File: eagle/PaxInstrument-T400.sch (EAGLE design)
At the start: 113 parts, among them IC1 MCP3424, J1 MICRO-SDCARD-CONNECTOR-330006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, U1 MCP9800, U3 MCP73831, U4 MIC5219-3.3V, U8 NC7S32, X1 FH12-12S-0.5SH, Y1 RESONATORSMD

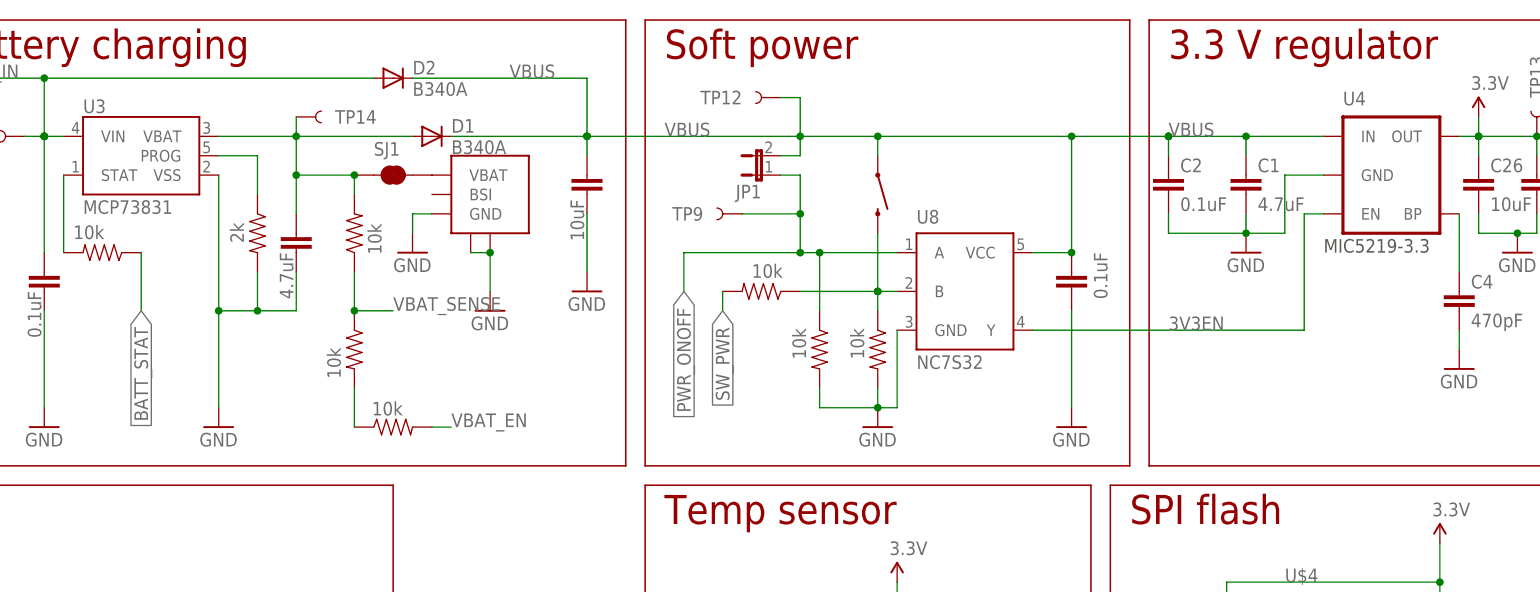
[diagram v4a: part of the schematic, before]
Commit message: Updated Rev 0.10 schematic and library
- What test points are needed? #37 (Added test point for BATT_STAT,
VBAT_SENSE, VBAT_EN -3V3EN in schematic)
- New soft power circuit #134 (Updated schematic only)
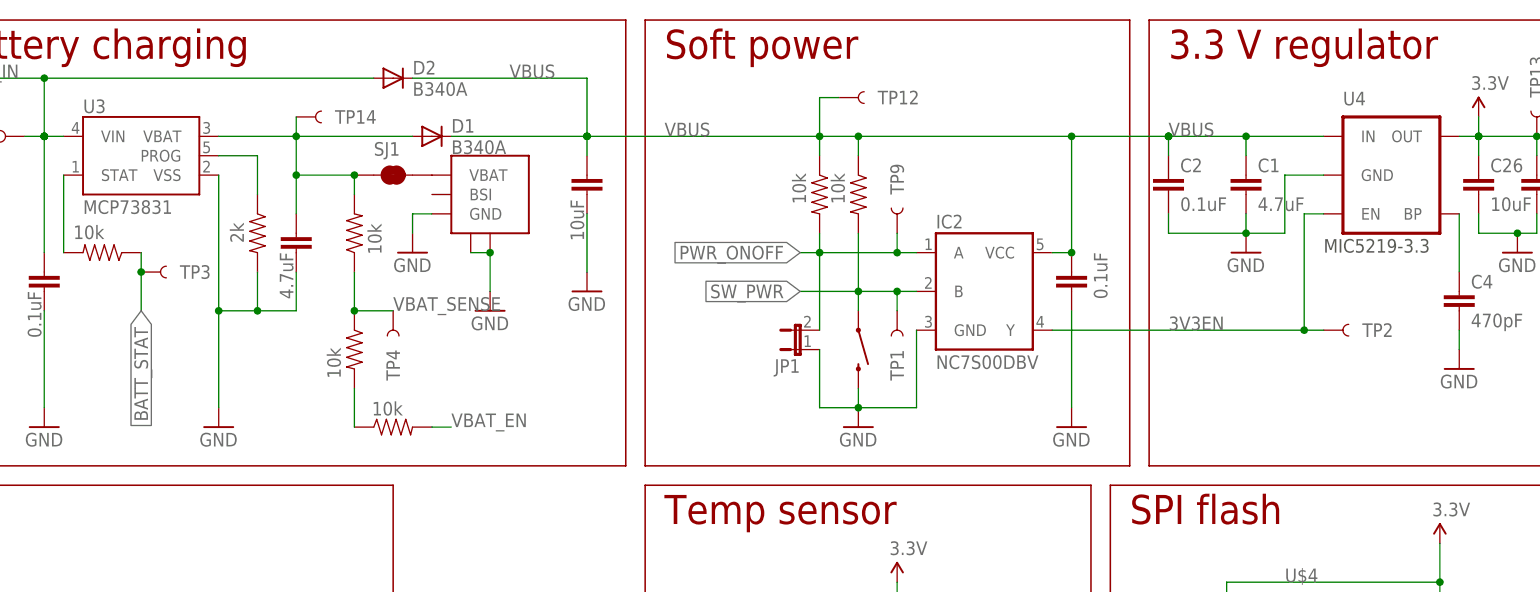
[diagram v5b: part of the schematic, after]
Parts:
- removed R1: 10k, PaxInstrument-T400:SPARKFUN-RESISTORS_RESISTOR0603-RES
- removed U8: NC7S32, SparkFun-DigitalIC:7432
- added IC2: NC7S00DBV, PaxInstrument-T400:NC7S00DBV
- added TP1, TP2, TP3, TP4: PWR_ON/OFF, PaxInstrument-T400:TEST-POINTTP_15TH_THRU
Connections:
- removed net N$99: R1.1, R6.1, S6.2, U8.B
- net 3V3EN: now also IC2.Y, TP2.1; no longer U8.Y
- net BATT_STAT: now also TP3.1
- net GND: now also IC2.GND, JP1.1, S6.2; no longer R6.2, R7.2, U8.GND
- net PWR_ONOFF: now also IC2.A, JP1.2, R7.2; no longer JP1.1, R7.1, U8.A
- net SW_PWR: now also IC2.B, R6.2, S6.1, TP1.1; no longer R1.2
- net VBAT_SENSE: now also TP4.1
- net VBUS: now also IC2.VCC, R6.1, R7.1; no longer JP1.2, S6.1, U8.VCC
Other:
- moved on the sheet: JP1, TP12, TP9

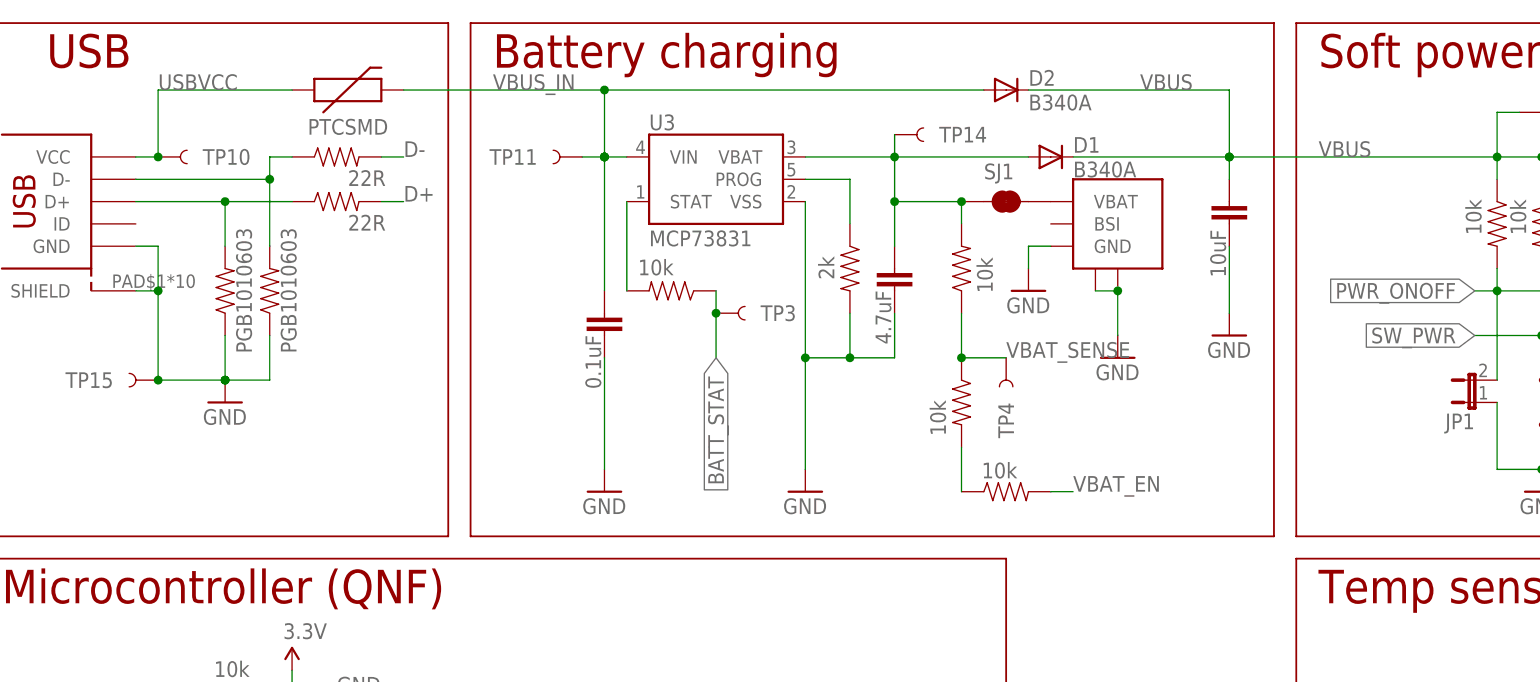
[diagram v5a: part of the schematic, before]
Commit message: Updated schematic for Rev 0.10
- see Use smaller diodes #14 (added supervision IC and Mosfet in Battery
charging circuit)
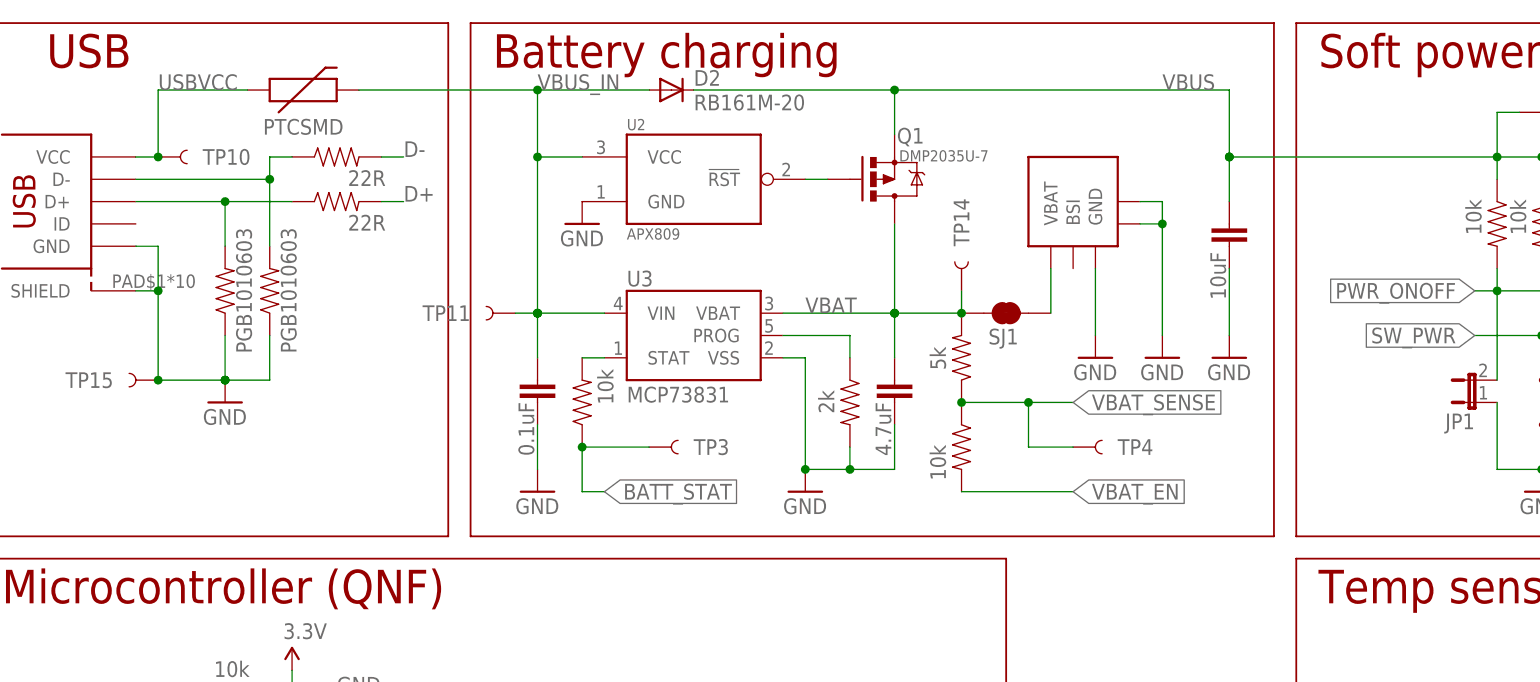
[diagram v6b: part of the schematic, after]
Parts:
- removed D1: B340A, SparkFun-DiscreteSemi:DIODESMA
- removed R25: 10k, PaxInstrument-T400:SPARKFUN-RESISTORS_RESISTOR0603-RES
- added Q1: DMP2035U-7, PaxInstrument-T400:MOSFET-PCHANNELSMD
- added U2: APX809, PaxInstrument-T400:APX809
- D2: value B340A -> RB161M-20; device SparkFun-DiscreteSemi:DIODESMA -> PaxInstrument-T400:SPARKFUN-DISCRETESEMI_DIODESOD123SOD123
- R20: value 10k -> 5k
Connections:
- removed net N$27: R24.2, R25.1
- new net N$12: Q1.G, U2.!RST
- net GND: now also U2.GND
- net VBAT: now also Q1.D; no longer D1.A
- net VBAT_EN: now also R24.2; no longer R25.2
- net VBUS: now also Q1.S; no longer D1.C
- net VBUS_IN: now also U2.VCC
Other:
- moved on the sheet: D2, SJ1, TP11, TP14, TP3, TP4, U3

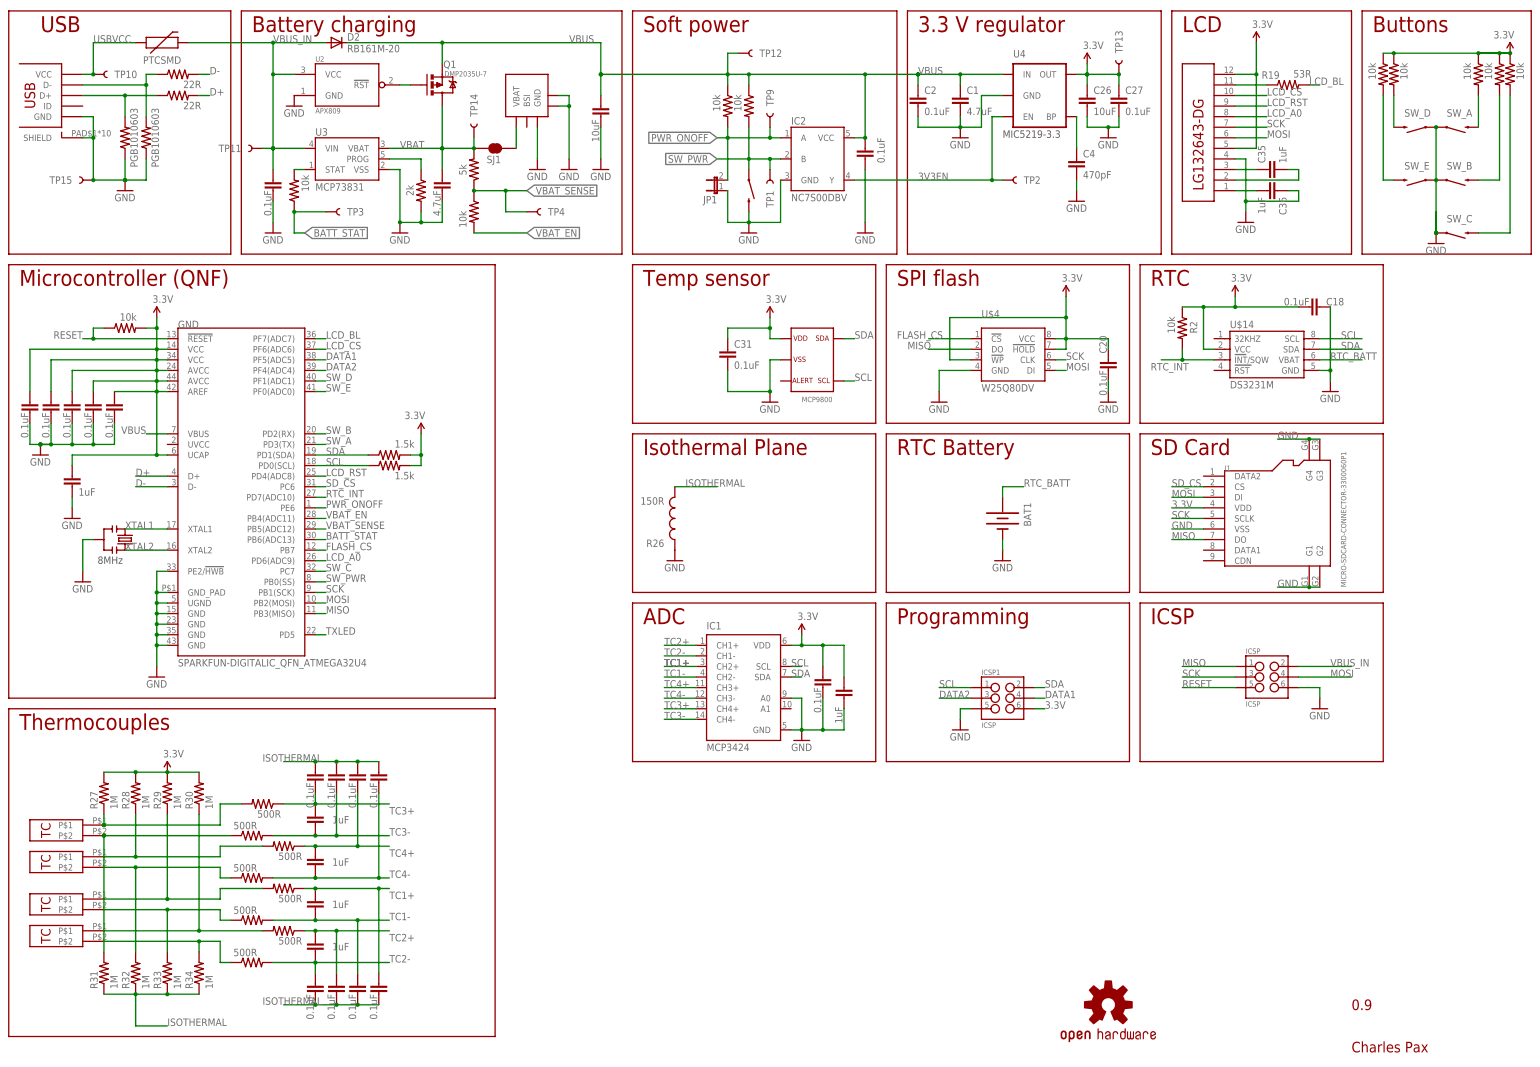
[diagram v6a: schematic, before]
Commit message: Updated for Rev 0.10
- Power on/off output low #118
- Adjust the thermal-couple connector width #138
- Add backlight test point #133
- Add FLASH_CS test point #132
- Add SD_CS test point #131
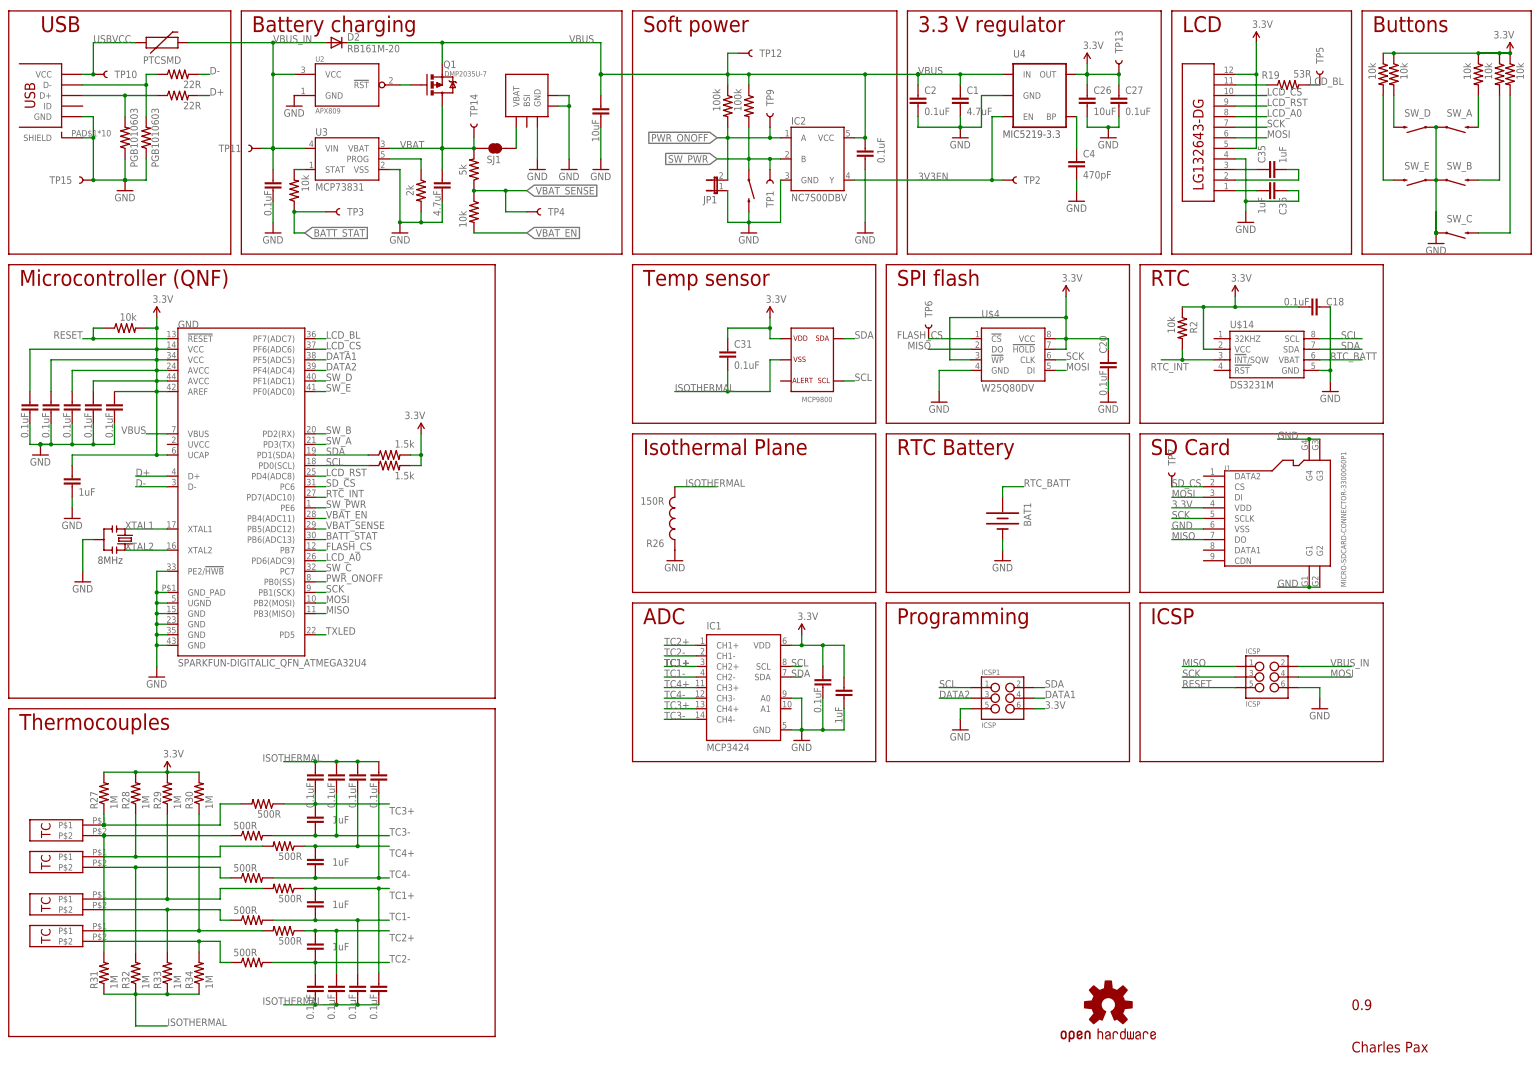
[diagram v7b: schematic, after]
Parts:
- added TP5, TP6, TP7: 3.3V, PaxInstrument-T400:TEST-POINTTP_15TH_THRU
- Q1: device PaxInstrument-T400:MOSFET-PCHANNELSMD -> PaxInstrument-T400:MOSFET-PCHANNELSMT
- R6, R7: value 10k -> 100k
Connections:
- net FLASH_CS: now also TP6.1
- net GND: no longer C31.2, U1.2
- net ISOTHERMAL: now also C31.2, U1.2
- net LCD_BL: now also TP5.1
- net PWR_ONOFF: now also GND.PB0(SS); no longer GND.PE6
- net SD_CS: now also TP7.1
- net SW_PWR: now also GND.PE6; no longer GND.PB0(SS)

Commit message: Updated for Rev 0.10
- Fixed Some capacitor still using 0805 package (Switch to 0603 #121)
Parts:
- C12, C26: device PaxInstrument-T400:SPARKFUN-CAPACITORS_CAP0805 -> PaxInstrument-T400:SPARKFUN-CAPACITORS_CAP0603-CAP
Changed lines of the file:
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@@
 <attribute name="OC_DIGIKEY" value="MCP73831T-2DCI/OTTR-ND"/>
 </part>
-<part name="C12" library="PaxInstrument-T400" deviceset="SPARKFUN-CAPACITORS_CAP" device="0805" value="10uF">
+<part name="C12" library="PaxInstrument-T400" deviceset="SPARKFUN-CAPACITORS_CAP" device="0603-CAP" value="10uF">
 <attribute name="MPN" value="JMK107ABJ106MAHT"/>
 <attribute name="OC_DIGIKEY" value="587-3383-2-ND"/>
@@
 </part>
 <part name="P+9" library="SparkFun" deviceset="3.3V" device=""/>
-<part name="C26" library="PaxInstrument-T400" deviceset="SPARKFUN-CAPACITORS_CAP" device="0805" value="10uF">
+<part name="C26" library="PaxInstrument-T400" deviceset="SPARKFUN-CAPACITORS_CAP" device="0603-CAP" value="10uF">
 <attribute name="MPN" value="JMK107ABJ106MAHT"/>
 <attribute name="OC_DIGIKEY" value="587-3383-2-ND"/>
